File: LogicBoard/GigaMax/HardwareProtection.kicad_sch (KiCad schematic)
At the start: 9 parts, among them U11 SN74LVC1G332DCKR

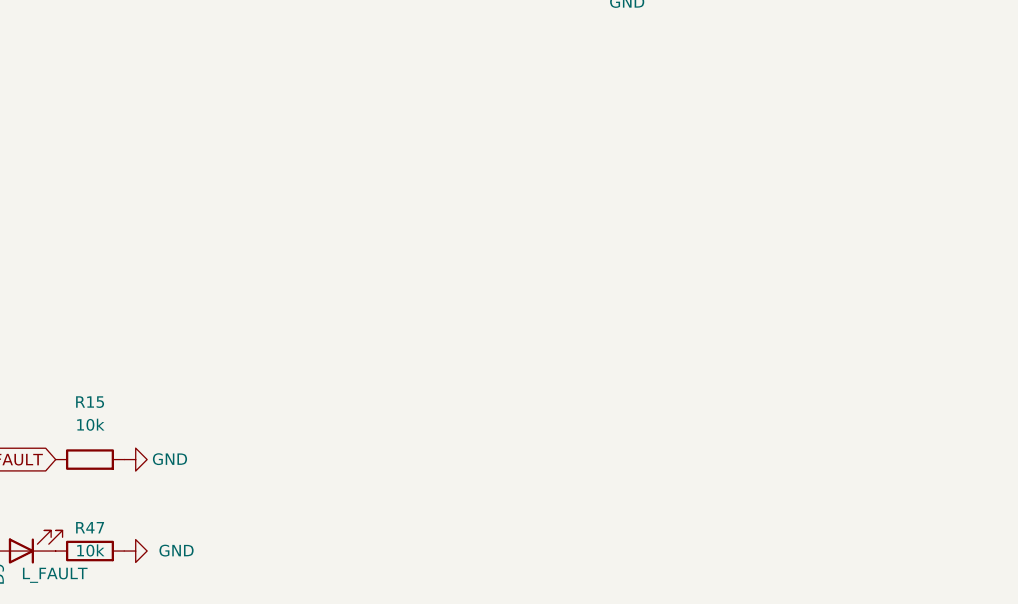
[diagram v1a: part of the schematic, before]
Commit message: v2.8.0 - Small Hall sensors
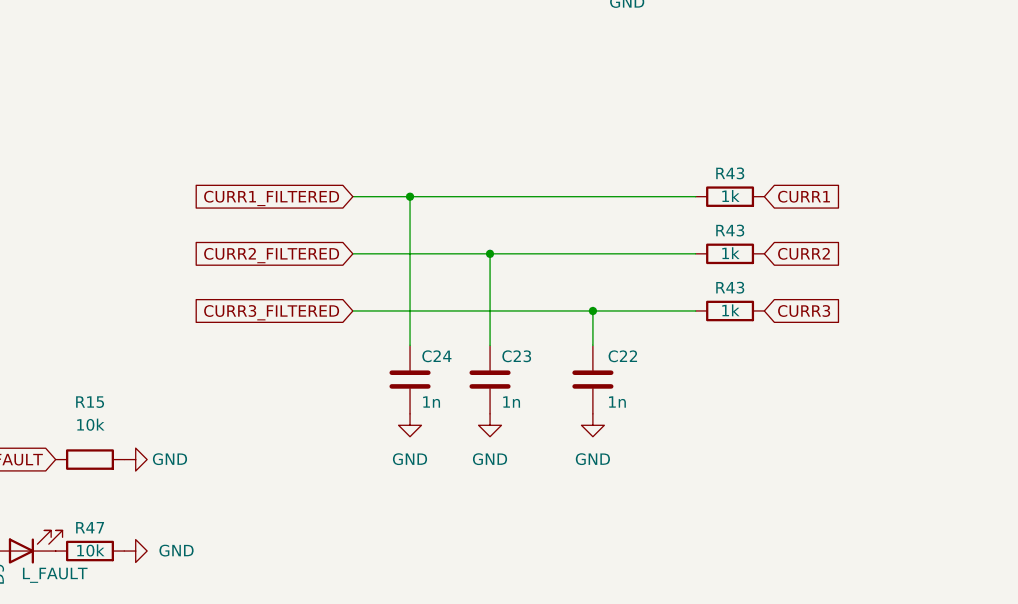
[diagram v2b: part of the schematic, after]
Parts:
- added C22, C23, C24: 1n, GigaVescLibs:C_0603_1608Metric_L, symbol Device:C
- added R43 (x3): 1k, Resistor_SMD:R_0603_1608Metric, symbol Device:R
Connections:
- net CURR1_FILTERED: now also C24.1, R43.1
- net CURR2_FILTERED: now also C23.1, R43.1
- net CURR3_FILTERED: now also C22.2, R43.1
- net GND: now also C22.1, C23.2, C24.2
- new net CURR1: R43.2
- new net CURR2: R43.2
- new net CURR3: R43.2
